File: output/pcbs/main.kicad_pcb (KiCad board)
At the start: 2 copper layers, 91.2 x 53.1 mm, 19 parts

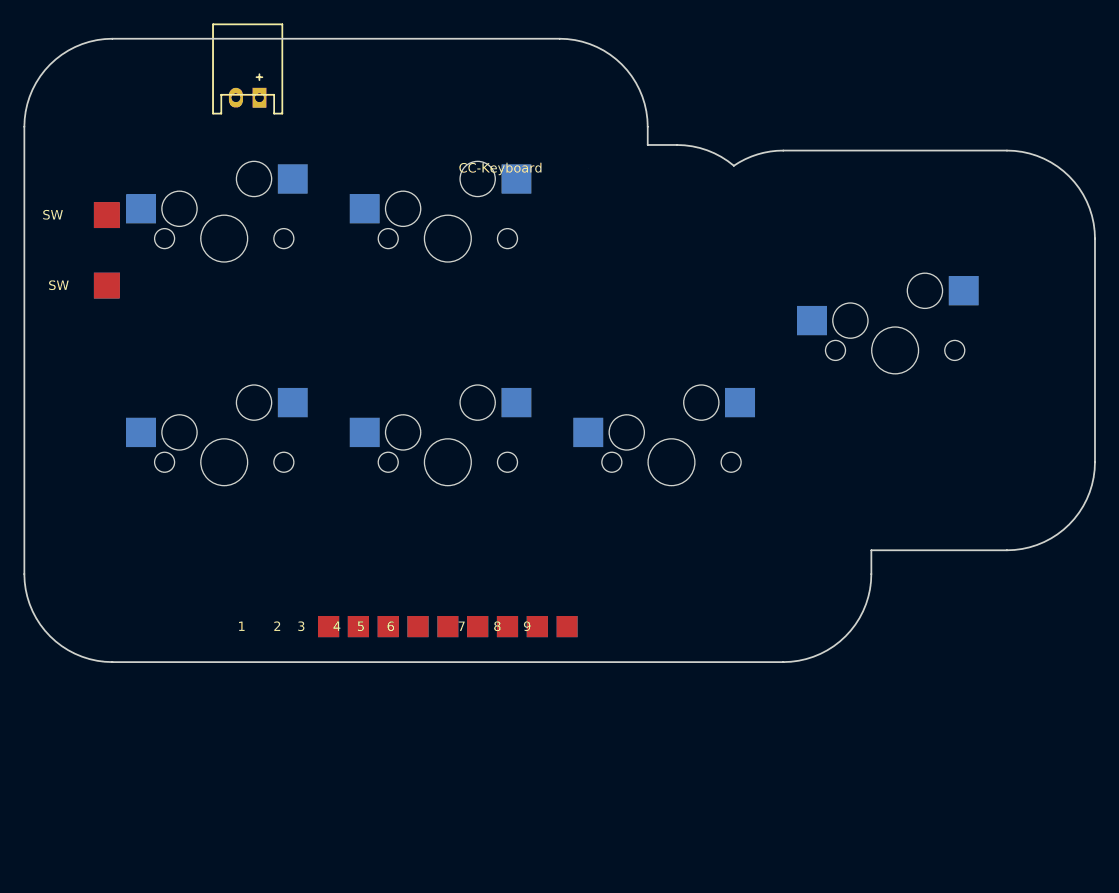
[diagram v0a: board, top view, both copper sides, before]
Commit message: PCB 加底部凸出区：SuperMini 躺平在板上（Pro Micro 兼容排母座）
- 板形加全宽 20mm 凸出区（91.2×70.7mm），定位板仍只含键阵不冲突
- 排母孔按 SuperMini/nice_nano_v2 pinout 摆双排（2.54 网格、排距 15.24），
  仅放用到的 9 孔，行B单孔天然防呆；pinout 经 kriscables 与 nice!nano v2
  两图交叉验证
- 修复：原 pin1-9 用 pad footprint 是贴片焊盘插不了排母，
  postprocess.py 转为 1.0mm 通孔（顺带固化数字规整/SVG 清理）
- 电池 JST、电源开关移入凸出区左右两段
- 接线表/BOM/焊接顺序同步更新
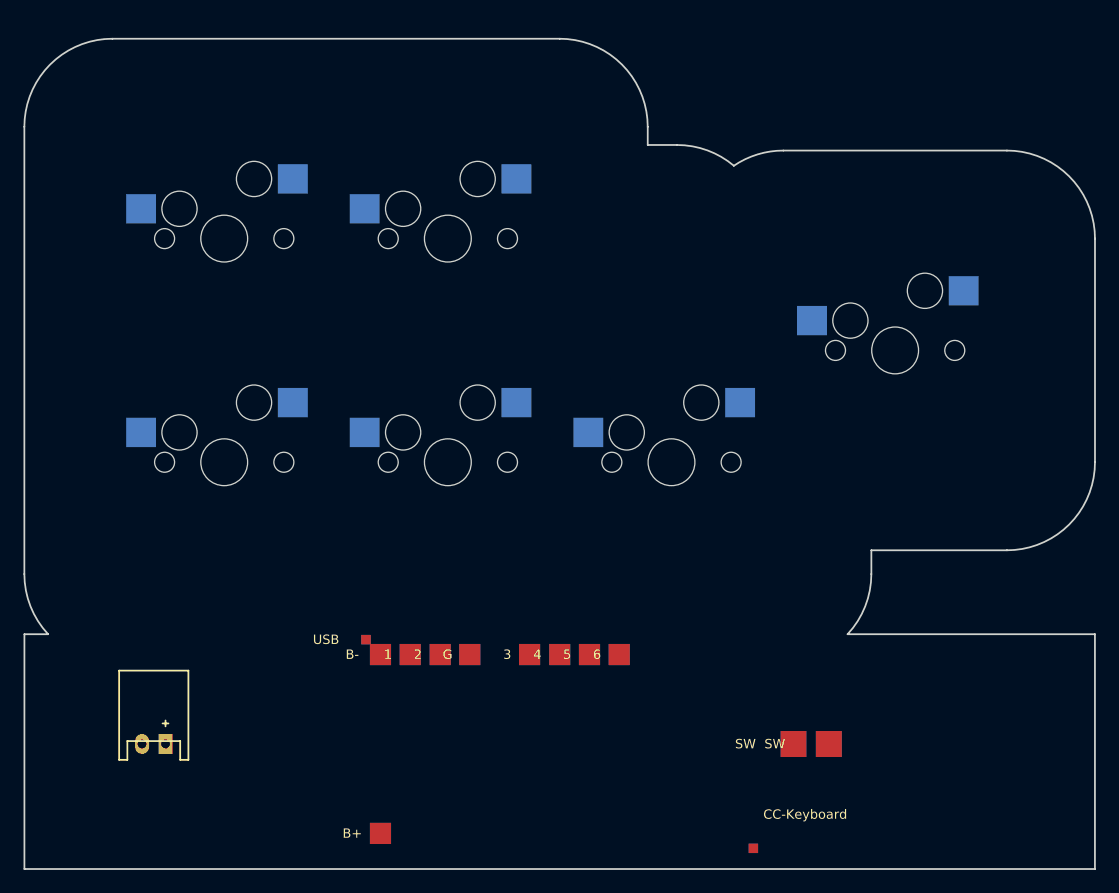
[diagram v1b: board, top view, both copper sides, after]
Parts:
- added PAD13: , SMDPad, F.Cu at (51.5, 24.0)
- added PAD14: , SMDPad, F.Cu at (58.0, 30.0)
- moved PAD11 77.1 mm to (45.1, 32.9)
- moved JST1 55.6 mm to (-6.00, 24.0)
- moved PAD12 52.1 mm to (48.5, 24.0)
- moved PAD10 37.4 mm to (12.1, 15.1)
- moved PAD9 23.7 mm to (13.3, 31.6)
- moved PAD6 7.38 mm to (28.6, 16.4)
- moved PAD7 7.38 mm to (31.1, 16.4)
- moved PAD8 7.38 mm to (33.7, 16.4)
- moved PAD5 7.36 mm to (26.0, 16.4)
- moved PAD2 5.02 mm to (15.9, 16.4)
- moved PAD1 5.02 mm to (13.3, 16.4)
- moved PAD3 5.02 mm to (18.4, 16.4)
- moved PAD4 5.02 mm to (20.9, 16.4)
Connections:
- PAD1 pad 1: KEY_ESC -> BAT_MINUS
- PAD10 pad 1: BAT_PLUS -> (no net)
- PAD11 pad 1: BAT_SWITCHED -> (no net)
- PAD12 pad 1: (no net) -> BAT_PLUS
- PAD2 pad 1: KEY_UP -> KEY_ESC
- PAD3 pad 1: KEY_LEFT -> KEY_UP
- PAD4 pad 1: KEY_DOWN -> GND
- PAD5 pad 1: KEY_RIGHT -> KEY_LEFT
- PAD6 pad 1: KEY_ENTER -> KEY_DOWN
- PAD7 pad 1: GND -> KEY_RIGHT
- PAD8 pad 1: BAT_SWITCHED -> KEY_ENTER
- PAD9 pad 1: BAT_MINUS -> BAT_SWITCHED
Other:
- board size 91.2 x 53.1 mm -> 91.2 x 70.7 mm

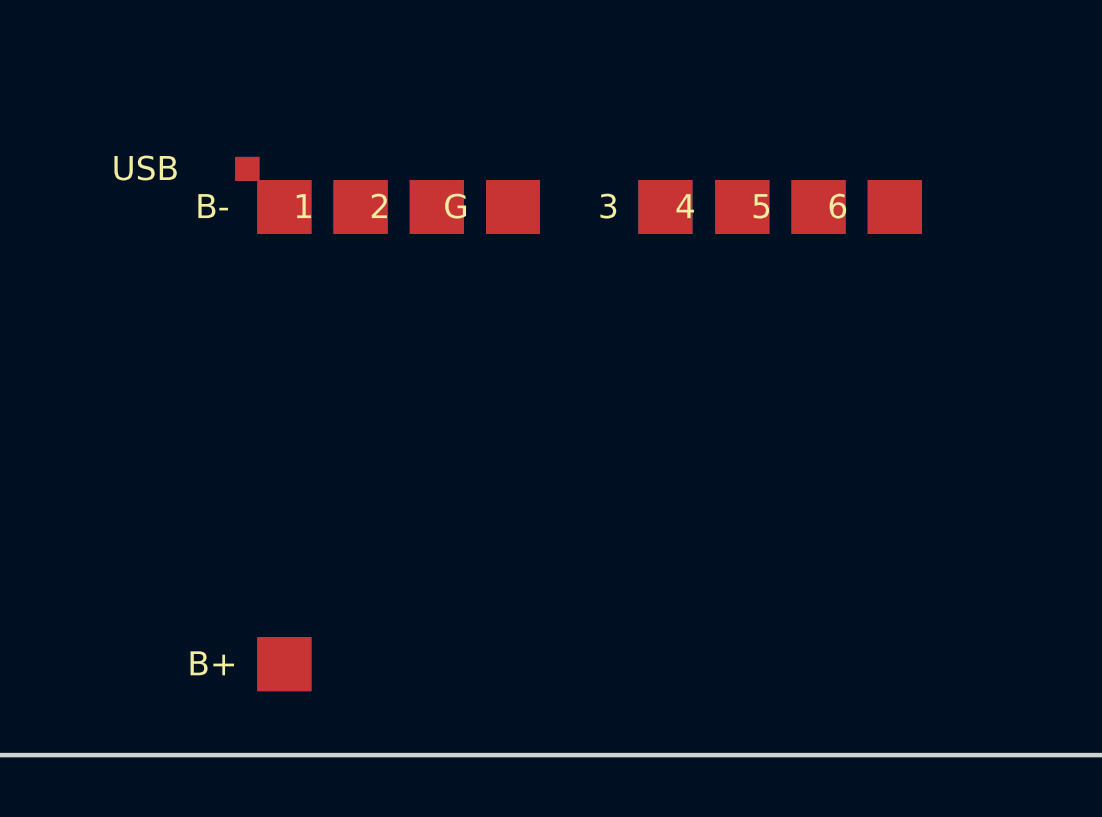
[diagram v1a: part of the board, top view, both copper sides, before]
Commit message: 排母孔位对齐实物 SuperMini（用户提供丝印）
实物每排 12 脚、排距 15.24：行A USB 端起 P0.06 P0.08 GND GND
P0.17 P0.20 P0.22 P0.24 ...（首位不是 B-，与 kriscables 版不同）。
原孔位整体错一格，已重排；该板无独立 B-，电池负极改并入 GND
（BAT_MINUS 网络移除）。行B 单孔 B+ 防呆保留。
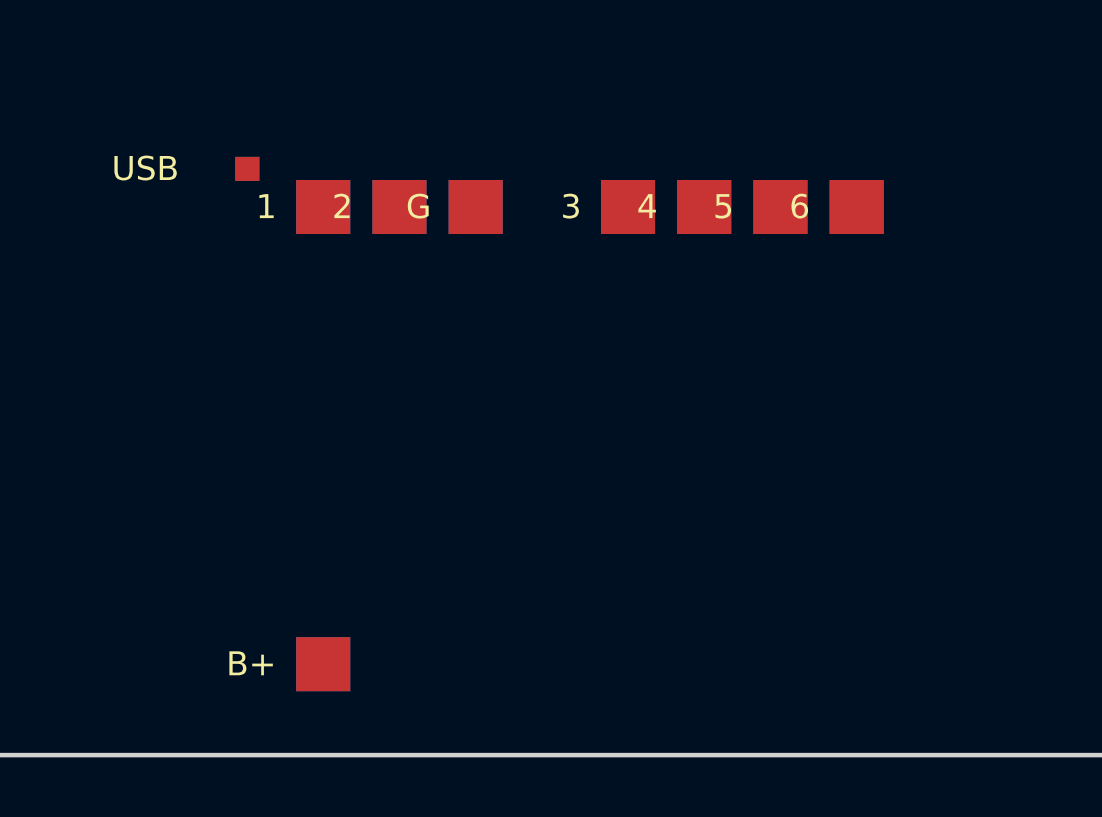
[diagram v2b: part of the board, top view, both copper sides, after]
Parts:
- removed PAD14: , SMDPad
- moved PAD10 37.5 mm to (45.1, 32.9)
- moved PAD8 24.4 mm to (14.6, 31.6)
- moved PAD9 16.6 mm to (12.1, 15.1)
- moved PAD11 9.53 mm to (48.5, 24.0)
- moved PAD13 8.85 mm to (58.0, 30.0)
- moved PAD4 3.84 mm to (24.8, 16.4)
- moved PAD12 3.00 mm to (51.5, 24.0)
- moved PAD3 1.30 mm to (19.7, 16.4)
- moved PAD1 1.29 mm to (14.6, 16.4)
- moved PAD2 1.29 mm to (17.1, 16.4)
- moved PAD5 1.29 mm to (27.3, 16.4)
- moved PAD7 1.27 mm to (32.4, 16.4)
- moved PAD6 1.27 mm to (29.8, 16.4)
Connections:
- JST1 pad 2: BAT_MINUS -> GND
- PAD1 pad 1: BAT_MINUS -> KEY_ESC
- PAD11 pad 1: (no net) -> BAT_PLUS
- PAD12 pad 1: BAT_PLUS -> BAT_SWITCHED
- PAD13 pad 1: BAT_SWITCHED -> (no net)
- PAD2 pad 1: KEY_ESC -> KEY_UP
- PAD3 pad 1: KEY_UP -> GND
- PAD4 pad 1: GND -> KEY_LEFT
- PAD5 pad 1: KEY_LEFT -> KEY_DOWN
- PAD6 pad 1: KEY_DOWN -> KEY_RIGHT
- PAD7 pad 1: KEY_RIGHT -> KEY_ENTER
- PAD8 pad 1: KEY_ENTER -> BAT_SWITCHED
- PAD9 pad 1: BAT_SWITCHED -> (no net)

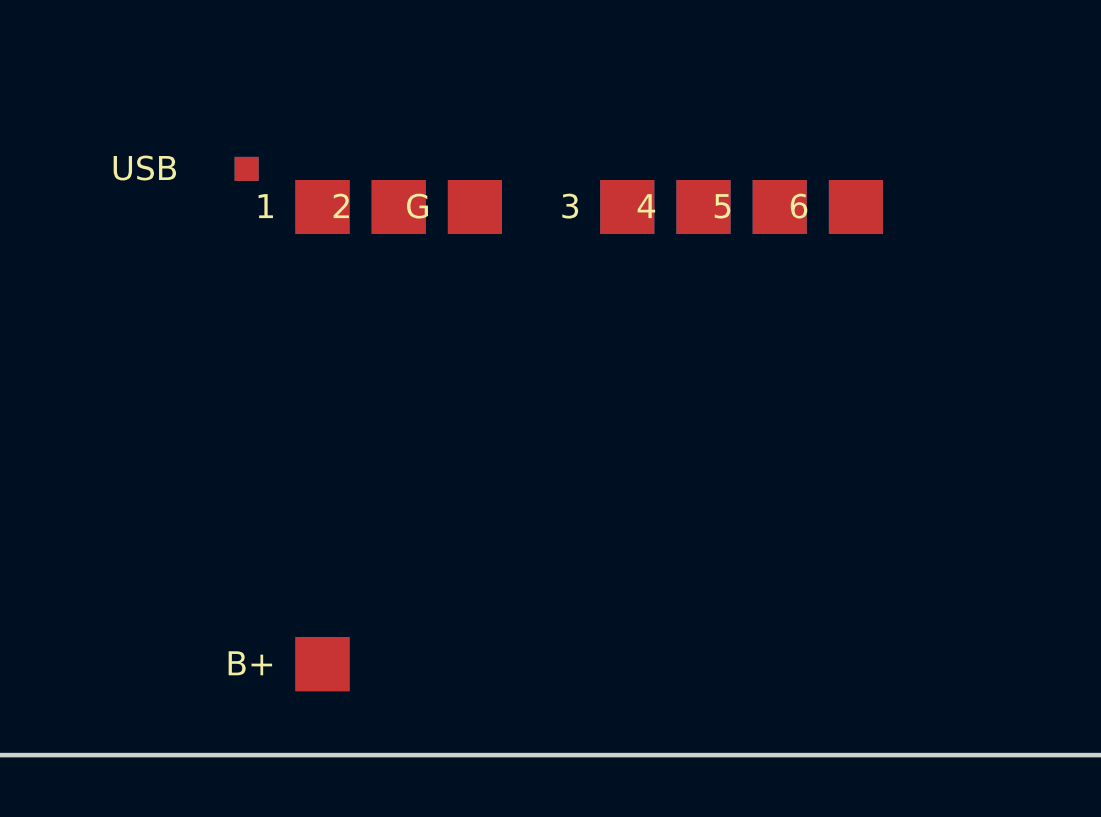
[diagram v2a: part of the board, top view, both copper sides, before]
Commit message: 排母孔位恢复 13×2 布局（用户确认每排 13 脚）
13 孔网格下排 1 首位为 B-（kriscables/nice!nano_v2 两图一致，
用户先前抄丝印漏了最边上的 B-）。B-/B+ 位于板端第一孔位，
BAT_MINUS 网络恢复，电池负极接 B-。
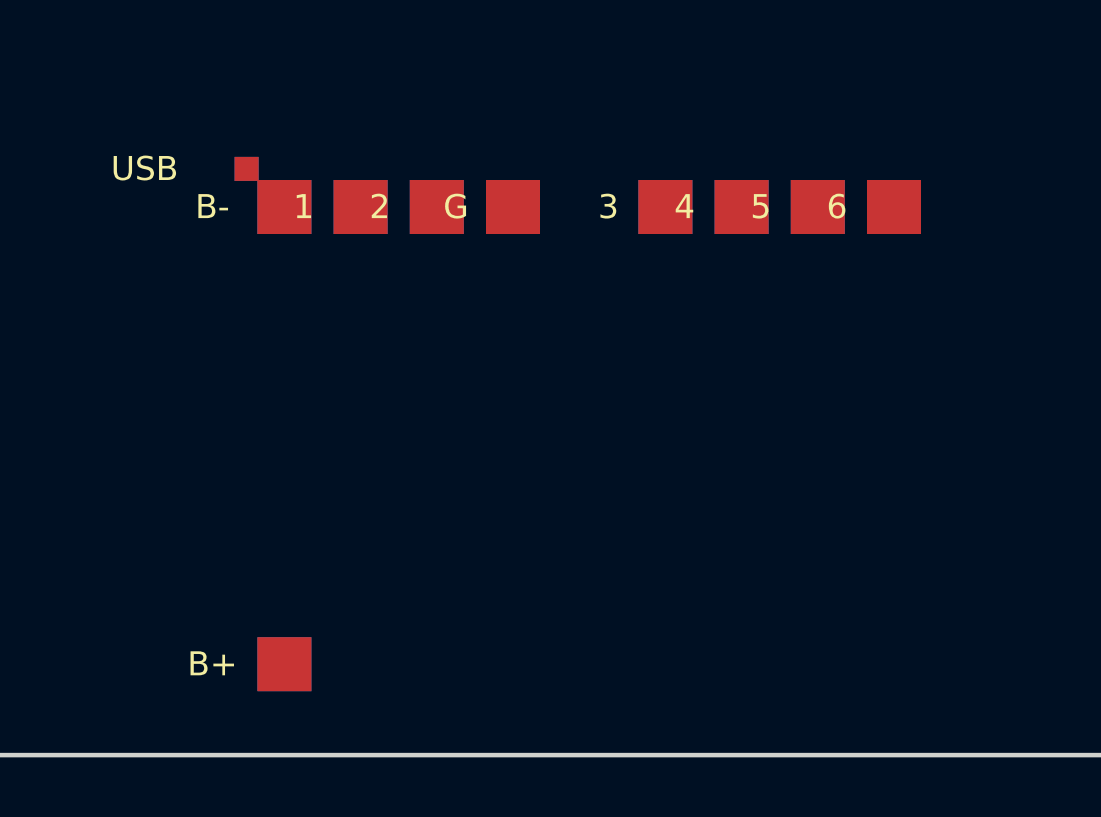
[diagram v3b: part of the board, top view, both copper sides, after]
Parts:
- added PAD14: , SMDPad, F.Cu at (58.0, 30.0)
- moved PAD10 37.5 mm to (12.1, 15.1)
- moved PAD8 24.4 mm to (33.7, 16.4)
- moved PAD9 16.6 mm to (13.3, 31.6)
- moved PAD11 9.53 mm to (45.1, 32.9)
- moved PAD13 8.85 mm to (51.5, 24.0)
- moved PAD4 3.81 mm to (21.0, 16.4)
- moved PAD12 3.00 mm to (48.5, 24.0)
- moved PAD3 1.27 mm to (18.4, 16.4)
- moved PAD7 1.27 mm to (31.1, 16.4)
- moved PAD1 1.27 mm to (13.3, 16.4)
- moved PAD2 1.27 mm to (15.9, 16.4)
- moved PAD5 1.27 mm to (26.0, 16.4)
- moved PAD6 1.27 mm to (28.6, 16.4)
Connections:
- JST1 pad 2: GND -> BAT_MINUS
- PAD1 pad 1: KEY_ESC -> BAT_MINUS
- PAD11 pad 1: BAT_PLUS -> (no net)
- PAD12 pad 1: BAT_SWITCHED -> BAT_PLUS
- PAD13 pad 1: (no net) -> BAT_SWITCHED
- PAD2 pad 1: KEY_UP -> KEY_ESC
- PAD3 pad 1: GND -> KEY_UP
- PAD4 pad 1: KEY_LEFT -> GND
- PAD5 pad 1: KEY_DOWN -> KEY_LEFT
- PAD6 pad 1: KEY_RIGHT -> KEY_DOWN
- PAD7 pad 1: KEY_ENTER -> KEY_RIGHT
- PAD8 pad 1: BAT_SWITCHED -> KEY_ENTER
- PAD9 pad 1: (no net) -> BAT_SWITCHED
